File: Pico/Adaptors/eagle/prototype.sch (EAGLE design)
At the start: 13 parts, among them J1 JST-2P-SMD-PW-3410050P1

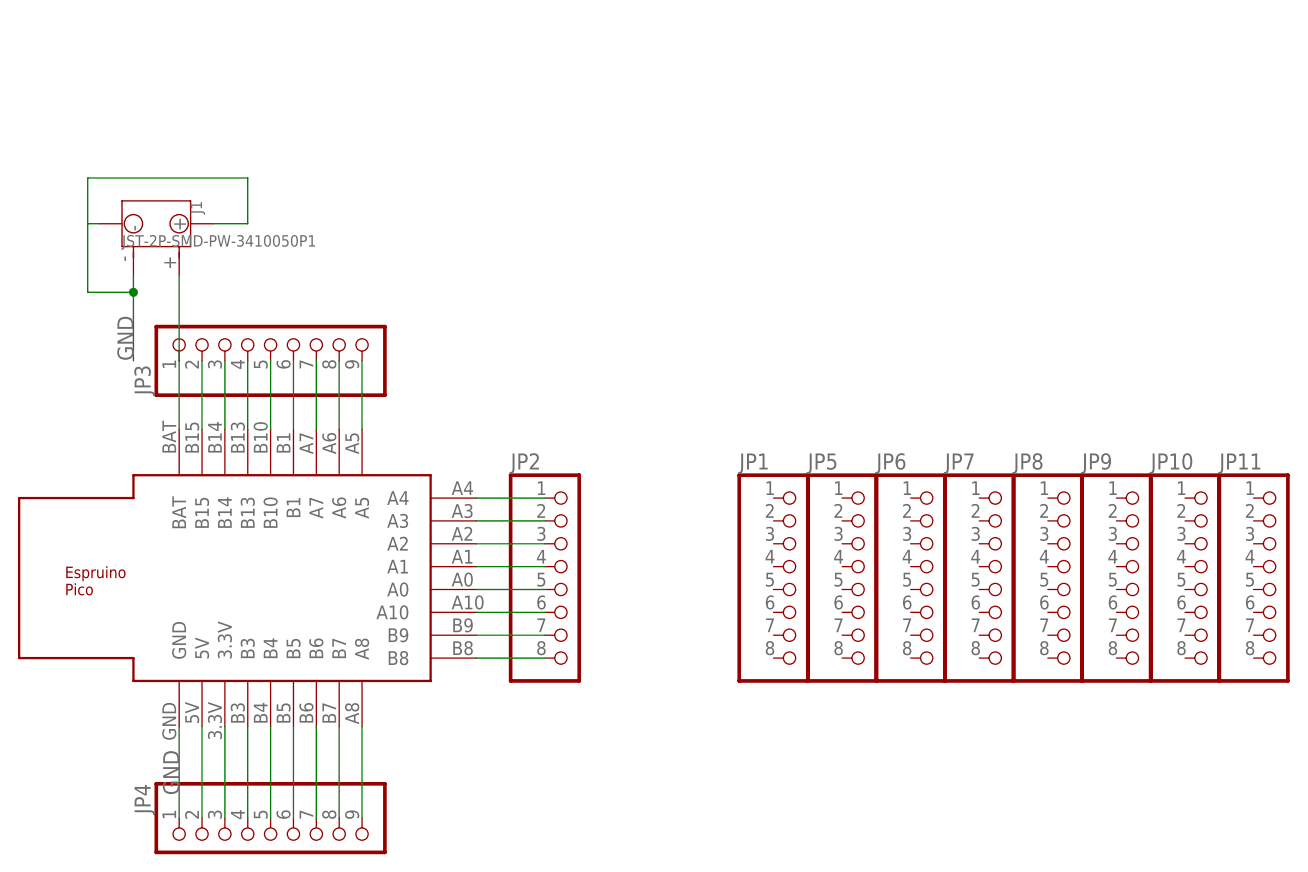
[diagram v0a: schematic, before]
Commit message: Added battery charger pads to proto headers
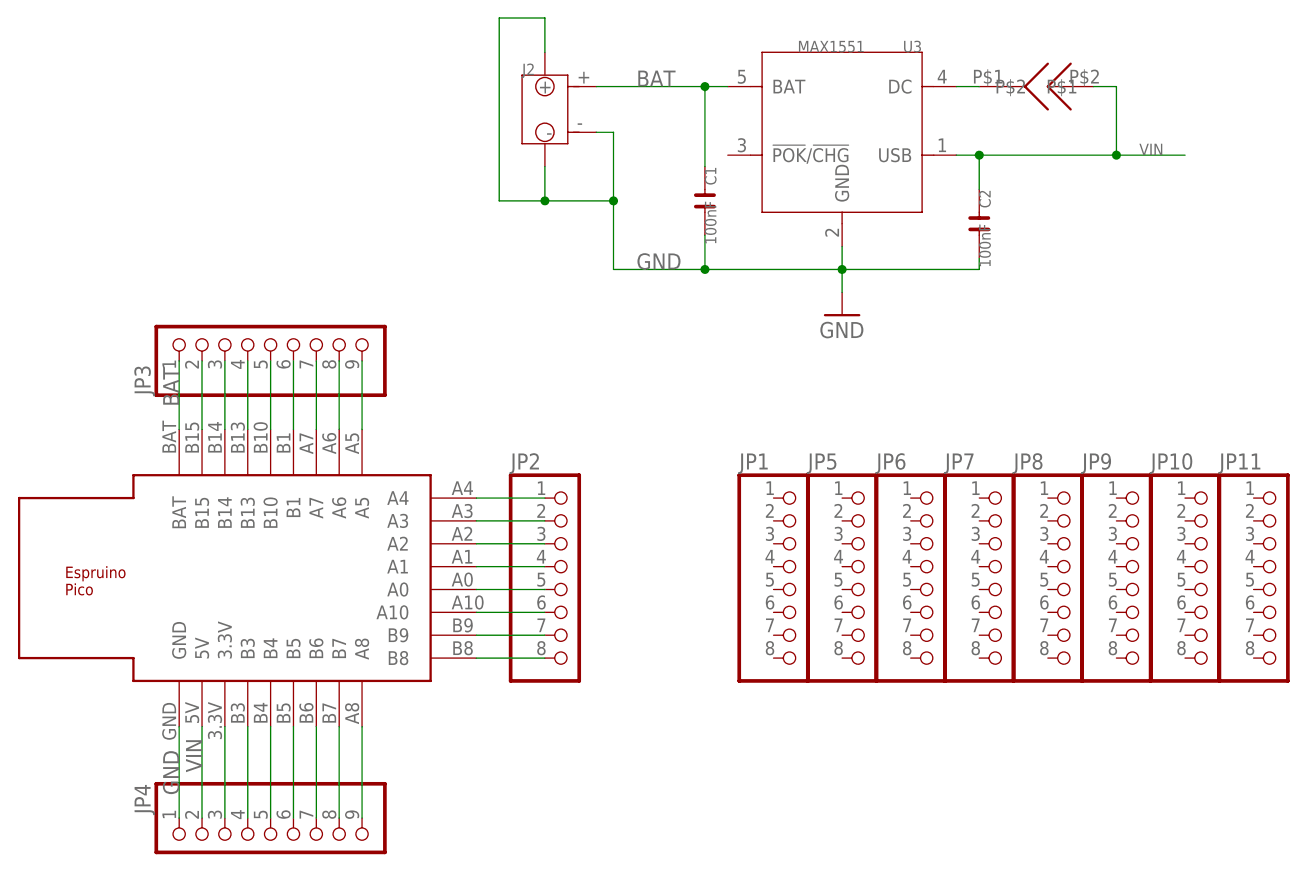
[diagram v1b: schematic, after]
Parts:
- removed J1: JST-2P-SMD-PW-3410050P1, OPL Eagle Library:JST-2P-SMD-PW-3410050P1
- added C1, C2: 100nF, OPL5:C-0603
- added J2: JST-2P-SMD-PW-3410050P1, OPL Eagle Library:JST-2P-SMD-PW-3410050P1
- added U$4: SOLDERJUMPER, solder_jumper:SOLDERJUMPER
- added U3: MAX1551, template:MAX1551
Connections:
- removed net 5V: JP4.2, U$1.5V
- removed net N$15: J1.+, JP3.1, U$1.BAT
- new net BAT: C1.1, J2.+, JP3.1, U$1.BAT, U3.BAT
- new net N$25: U$4.P$1, U3.DC
- new net VIN: C2.1, JP4.2, U$1.5V, U$4.P$2, U3.USB
- net GND: now also C1.2, C2.2, J2.-, J2.3, J2.4, U3.GND; no longer J1.-, J1.3, J1.4
